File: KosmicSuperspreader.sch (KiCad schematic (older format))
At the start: 22 parts

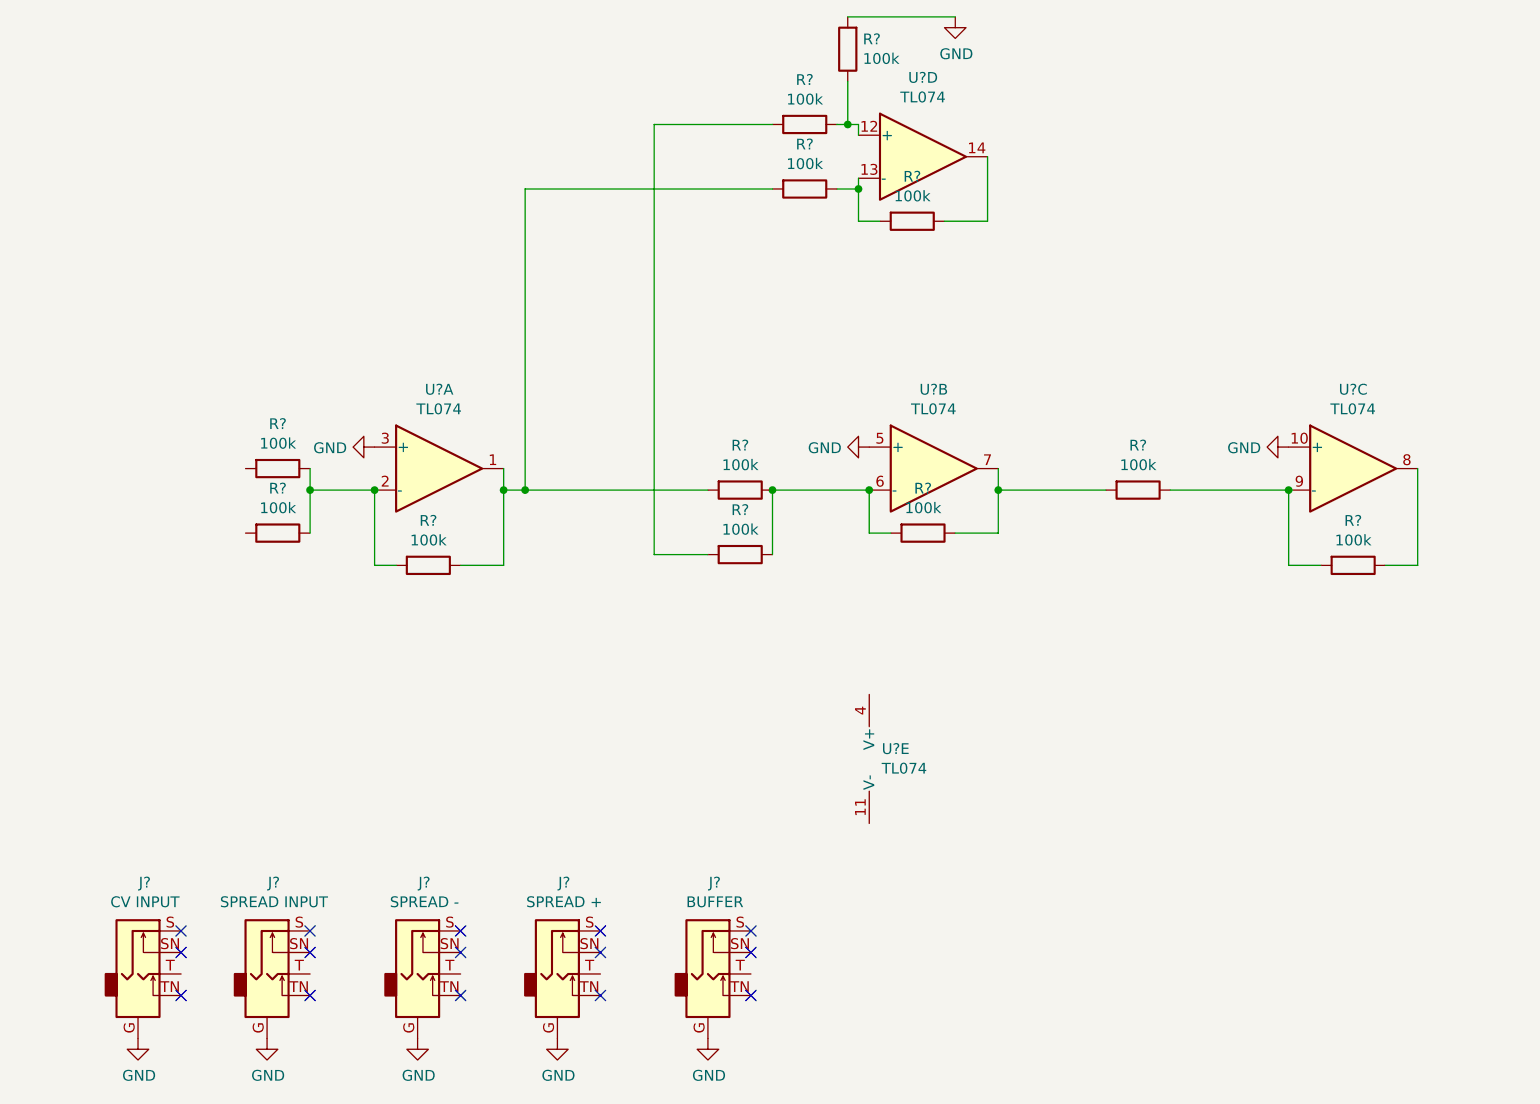
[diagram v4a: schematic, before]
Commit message: Pots and labels
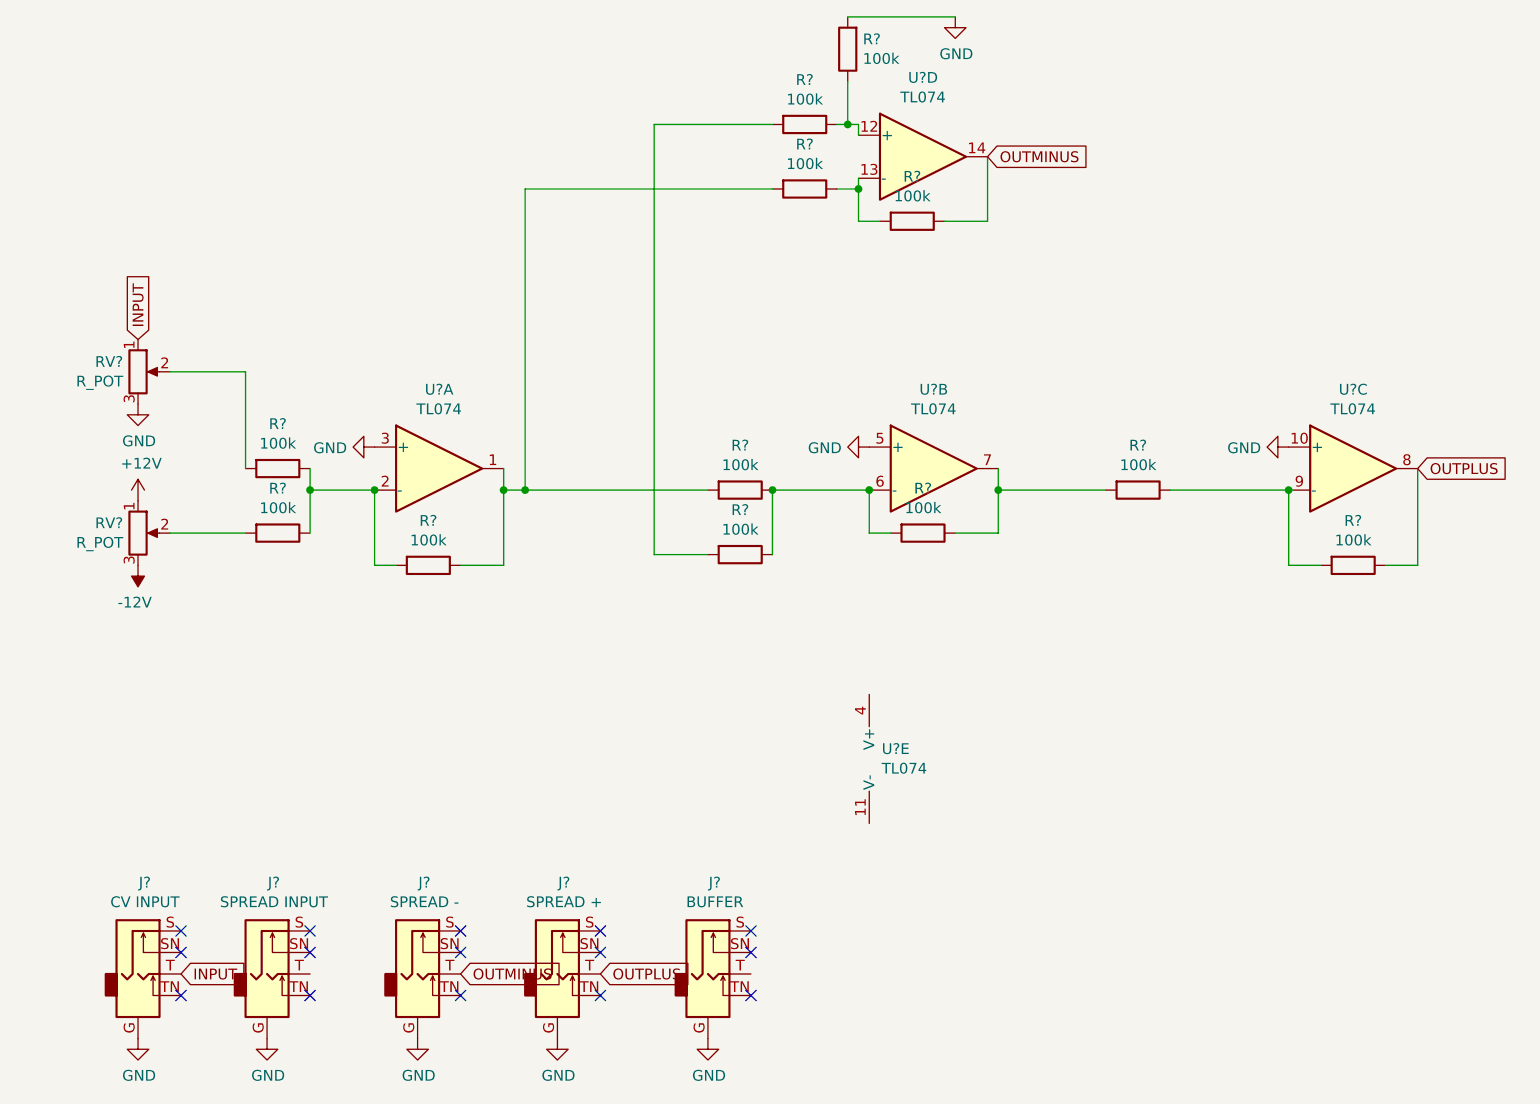
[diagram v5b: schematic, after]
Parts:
- added RV? (x2): R_POT, symbol Device:R_POT
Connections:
- net GND: now also RV?.3
- net OUTPLUS: now reaches R?.1, U?.8
- net OUTPLUS: now also J?.T
- net OUTMINUS: now reaches R?.1, U?.14
- net OUTMINUS: now also J?.T
- net at R?.2: now also RV?.2 (x2)
- net INPUT: now reaches J?.T
- net INPUT: now also RV?.1
- new net +12V: RV?.1
- new net -12V: RV?.3
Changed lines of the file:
@@
 	1    0    0    -1
 $EndComp
+$Comp
+L Device:R_POT RV?
+U 1 1 60B37DC5
+P 1600 4300
+F 0 "RV?" H 1531 4346 50  0000 R CNN
+F 1 "R_POT" H 1531 4255 50  0000 R CNN
+F 2 "" H 1600 4300 50  0001 C CNN
+F 3 "~" H 1600 4300 50  0001 C CNN
+	1    1600 4300
+	1    0    0    -1
+$EndComp
+Text GLabel 7550 4000 2    50   Input ~ 0
+OUTPLUS
+Text GLabel 3750 6350 2    50   Input ~ 0
+OUTPLUS
+Text GLabel 5550 2550 2    50   Input ~ 0
+OUTMINUS
+Text GLabel 3100 6350 2    50   Input ~ 0
+OUTMINUS
+$Comp
+L power:-12V #PWR?
+U 1 1 60B39192
+P 1600 4450
+F 0 "#PWR?" H 1600 4550 50  0001 C CNN
+F 1 "-12V" H 1615 4623 50  0000 C CNN
+F 2 "" H 1600 4450 50  0001 C CNN
+F 3 "" H 1600 4450 50  0001 C CNN
+	1    1600 4450
+	-1   0    0    1
+$EndComp
+$Comp
+L power:+12V #PWR?
+U 1 1 60B39B80
+P 1600 4150
+F 0 "#PWR?" H 1600 4000 50  0001 C CNN
+F 1 "+12V" H 1615 4323 50  0000 C CNN
+F 2 "" H 1600 4150 50  0001 C CNN
+F 3 "" H 1600 4150 50  0001 C CNN
+	1    1600 4150
+	1    0    0    -1
+$EndComp
+Wire Wire Line
+	2100 4300 1750 4300
+$Comp
+L Device:R_POT RV?
+U 1 1 60B3AD55
+P 1600 3550
+F 0 "RV?" H 1531 3596 50  0000 R CNN
+F 1 "R_POT" H 1531 3505 50  0000 R CNN
+F 2 "" H 1600 3550 50  0001 C CNN
+F 3 "~" H 1600 3550 50  0001 C CNN
+	1    1600 3550
+	1    0    0    -1
+$EndComp
+$Comp
+L power:GND #PWR?
+U 1 1 60B3B35D
+P 1600 3700
+F 0 "#PWR?" H 1600 3450 50  0001 C CNN
+F 1 "GND" H 1605 3527 50  0000 C CNN
+F 2 "" H 1600 3700 50  0001 C CNN
+F 3 "" H 1600 3700 50  0001 C CNN
+	1    1600 3700
+	1    0    0    -1
+$EndComp
+Text GLabel 1600 3400 1    50   Input ~ 0
+INPUT
+Text GLabel 1800 6350 2    50   Input ~ 0
+INPUT
+Wire Wire Line
+	1750 3550 2100 3550
+Wire Wire Line
+	2100 3550 2100 4000
 $EndSCHEMATC

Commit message: Change jacks, fix labels
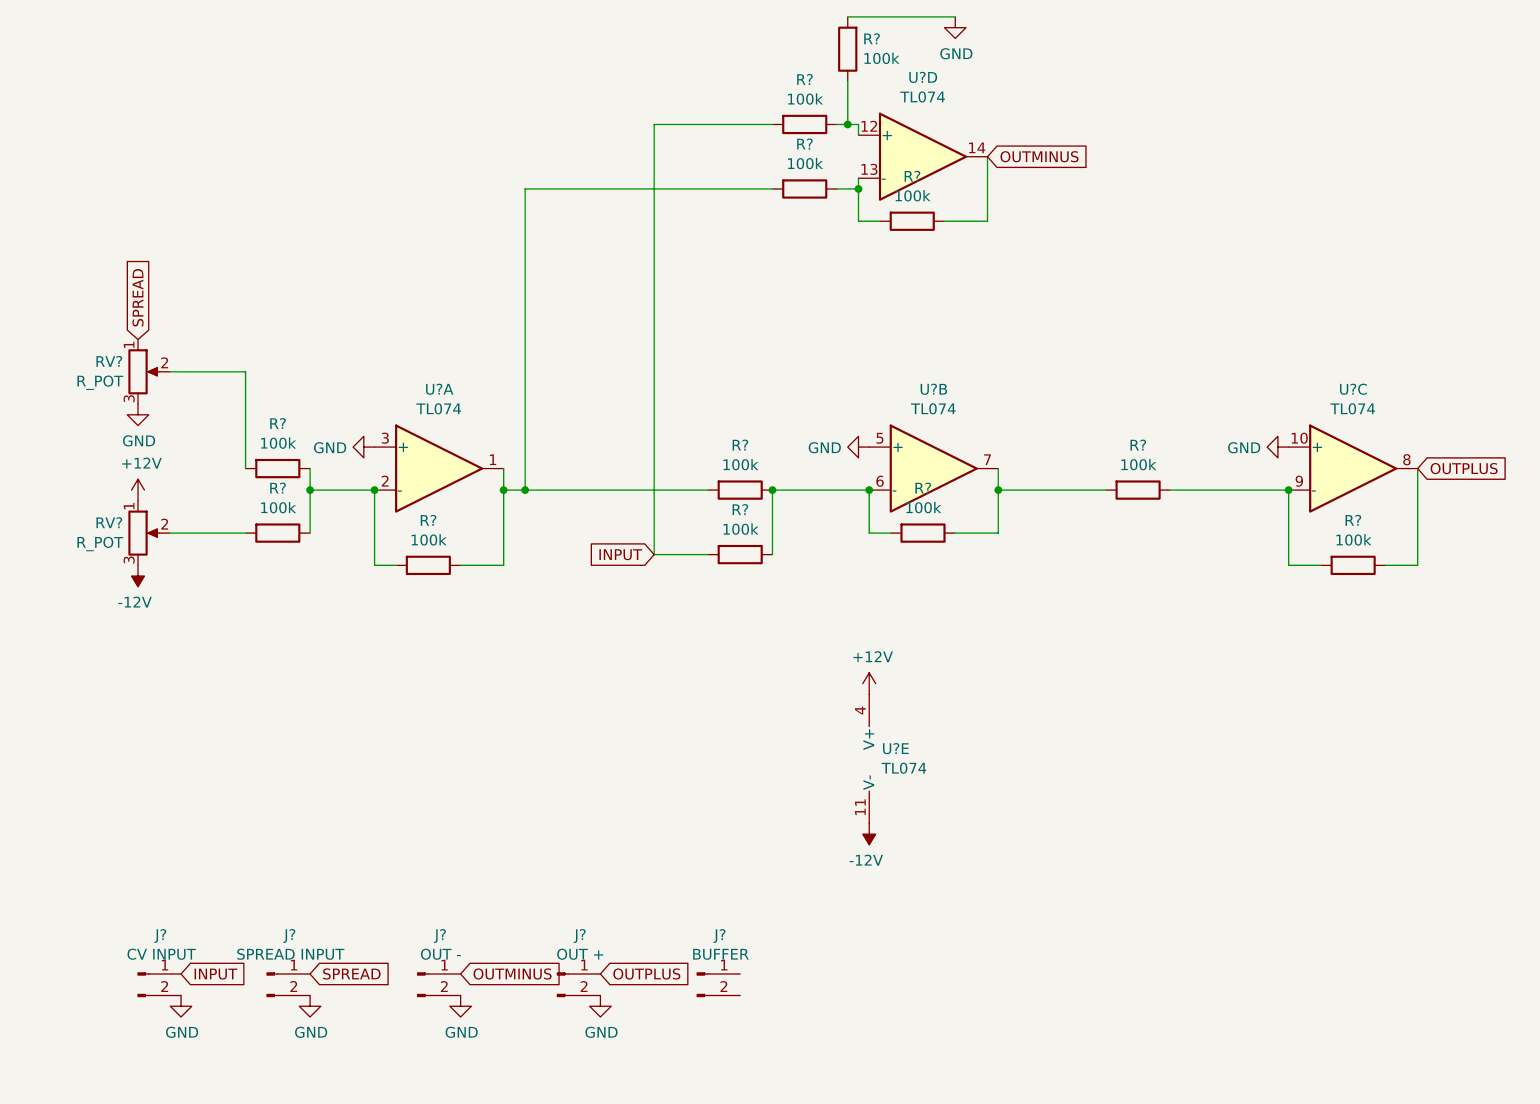
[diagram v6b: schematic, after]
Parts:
- removed J?: SPREAD INPUT, symbol Connector:AudioJack2_Ground_Switch
- removed J?: SPREAD -, symbol Connector:AudioJack2_Ground_Switch
- removed J?: SPREAD +, symbol Connector:AudioJack2_Ground_Switch
- removed J?: BUFFER, symbol Connector:AudioJack2_Ground_Switch
- removed J?: CV INPUT, symbol Connector:AudioJack2_Ground_Switch
- added J?: CV INPUT, symbol Connector:Conn_01x02_Male
- added J?: SPREAD INPUT, symbol Connector:Conn_01x02_Male
- added J?: OUT -, symbol Connector:Conn_01x02_Male
- added J?: OUT +, symbol Connector:Conn_01x02_Male
- added J?: BUFFER, symbol Connector:Conn_01x02_Male
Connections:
- net +12V: now also U?.4 (V+)
- net -12V: now also U?.11 (V-)
- net GND: now also J?.2 (Pin_2), J?.2 (Pin_2), J?.2 (Pin_2), J?.2 (Pin_2)
- net INPUT: now also R?.2, R?.2, J?.1 (Pin_1); no longer RV?.1
- net OUTMINUS: now also J?.1 (Pin_1)
- net OUTPLUS: now also J?.1 (Pin_1)
- new net SPREAD: J?.1 (Pin_1), RV?.1
- no-connect marks 15 -> 0
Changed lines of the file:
@@
 	4000 2400 4550 2400
 $Comp
-L Connector:AudioJack2_Ground_Switch J?
-U 1 1 60B2E747
-P 2200 6350
-F 0 "J?" H 2232 6775 50  0000 C CNN
-F 1 "SPREAD INPUT" H 2232 6684 50  0000 C CNN
-F 2 "" H 2200 6550 50  0001 C CNN
-F 3 "~" H 2200 6550 50  0001 C CNN
-F 4 "A-1121" H 2200 6350 50  0001 C CNN "Part"
-	1    2200 6350
-	1    0    0    -1
-$EndComp
-NoConn ~ 2400 6450
-NoConn ~ 2400 6250
-NoConn ~ 2400 6150
-$Comp
-L power:GND #PWR?
-U 1 1 60B30BB2
-P 2200 6650
-F 0 "#PWR?" H 2200 6400 50  0001 C CNN
-F 1 "GND" H 2205 6477 50  0000 C CNN
-F 2 "" H 2200 6650 50  0001 C CNN
-F 3 "" H 2200 6650 50  0001 C CNN
-	1    2200 6650
-	1    0    0    -1
-$EndComp
-$Comp
-L Connector:AudioJack2_Ground_Switch J?
-U 1 1 60B31450
-P 2900 6350
-F 0 "J?" H 2932 6775 50  0000 C CNN
-F 1 "SPREAD -" H 2932 6684 50  0000 C CNN
-F 2 "" H 2900 6550 50  0001 C CNN
-F 3 "~" H 2900 6550 50  0001 C CNN
-F 4 "A-1121" H 2900 6350 50  0001 C CNN "Part"
-	1    2900 6350
-	1    0    0    -1
-$EndComp
-NoConn ~ 3100 6450
-NoConn ~ 3100 6250
-NoConn ~ 3100 6150
-$Comp
-L power:GND #PWR?
-U 1 1 60B31769
-P 2900 6650
-F 0 "#PWR?" H 2900 6400 50  0001 C CNN
-F 1 "GND" H 2905 6477 50  0000 C CNN
-F 2 "" H 2900 6650 50  0001 C CNN
-F 3 "" H 2900 6650 50  0001 C CNN
-	1    2900 6650
-	1    0    0    -1
-$EndComp
-$Comp
-L Connector:AudioJack2_Ground_Switch J?
-U 1 1 60B33779
-P 3550 6350
-F 0 "J?" H 3582 6775 50  0000 C CNN
-F 1 "SPREAD +" H 3582 6684 50  0000 C CNN
-F 2 "" H 3550 6550 50  0001 C CNN
-F 3 "~" H 3550 6550 50  0001 C CNN
-F 4 "A-1121" H 3550 6350 50  0001 C CNN "Part"
-	1    3550 6350
-	1    0    0    -1
-$EndComp
-NoConn ~ 3750 6450
-NoConn ~ 3750 6250
-NoConn ~ 3750 6150
-$Comp
-L power:GND #PWR?
-U 1 1 60B33AC2
-P 3550 6650
-F 0 "#PWR?" H 3550 6400 50  0001 C CNN
-F 1 "GND" H 3555 6477 50  0000 C CNN
-F 2 "" H 3550 6650 50  0001 C CNN
-F 3 "" H 3550 6650 50  0001 C CNN
-	1    3550 6650
-	1    0    0    -1
-$EndComp
-$Comp
-L Connector:AudioJack2_Ground_Switch J?
-U 1 1 60B33ACD
-P 4250 6350
-F 0 "J?" H 4282 6775 50  0000 C CNN
-F 1 "BUFFER" H 4282 6684 50  0000 C CNN
-F 2 "" H 4250 6550 50  0001 C CNN
-F 3 "~" H 4250 6550 50  0001 C CNN
-F 4 "A-1121" H 4250 6350 50  0001 C CNN "Part"
-	1    4250 6350
-	1    0    0    -1
-$EndComp
-NoConn ~ 4450 6450
-NoConn ~ 4450 6250
-NoConn ~ 4450 6150
-$Comp
-L power:GND #PWR?
-U 1 1 60B33ADA
-P 4250 6650
-F 0 "#PWR?" H 4250 6400 50  0001 C CNN
-F 1 "GND" H 4255 6477 50  0000 C CNN
-F 2 "" H 4250 6650 50  0001 C CNN
-F 3 "" H 4250 6650 50  0001 C CNN
-	1    4250 6650
-	1    0    0    -1
-$EndComp
-$Comp
-L Connector:AudioJack2_Ground_Switch J?
-U 1 1 60B3629C
-P 1600 6350
-F 0 "J?" H 1632 6775 50  0000 C CNN
-F 1 "CV INPUT" H 1632 6684 50  0000 C CNN
-F 2 "" H 1600 6550 50  0001 C CNN
-F 3 "~" H 1600 6550 50  0001 C CNN
-F 4 "A-1121" H 1600 6350 50  0001 C CNN "Part"
-	1    1600 6350
-	1    0    0    -1
-$EndComp
-NoConn ~ 1800 6450
-NoConn ~ 1800 6250
-NoConn ~ 1800 6150
-$Comp
 L power:GND #PWR?
 U 1 1 60B36645
-P 1600 6650
-F 0 "#PWR?" H 1600 6400 50  0001 C CNN
-F 1 "GND" H 1605 6477 50  0000 C CNN
-F 2 "" H 1600 6650 50  0001 C CNN
-F 3 "" H 1600 6650 50  0001 C CNN
-	1    1600 6650
+P 1800 6450
+F 0 "#PWR?" H 1800 6200 50  0001 C CNN
+F 1 "GND" H 1805 6277 50  0000 C CNN
+F 2 "" H 1800 6450 50  0001 C CNN
+F 3 "" H 1800 6450 50  0001 C CNN
+	1    1800 6450
 	1    0    0    -1
 $EndComp
@@
 Text GLabel 7550 4000 2    50   Input ~ 0
 OUTPLUS
-Text GLabel 3750 6350 2    50   Input ~ 0
-OUTPLUS
 Text GLabel 5550 2550 2    50   Input ~ 0
-OUTMINUS
-Text GLabel 3100 6350 2    50   Input ~ 0
 OUTMINUS
 $Comp
@@
 	1    0    0    -1
 $EndComp
-Text GLabel 1600 3400 1    50   Input ~ 0
-INPUT
-Text GLabel 1800 6350 2    50   Input ~ 0
-INPUT
 Wire Wire Line
 	1750 3550 2100 3550
 Wire Wire Line
 	2100 3550 2100 4000
+Text GLabel 1800 6350 2    50   Input ~ 0
+INPUT
+Text GLabel 3100 6350 2    50   Input ~ 0
+OUTMINUS
+Text GLabel 3750 6350 2    50   Input ~ 0
+OUTPLUS
+$Comp
+L Connector:Conn_01x02_Male J?
+U 1 1 60B41A70
+P 1600 6350
+F 0 "J?" H 1708 6531 50  0000 C CNN
+F 1 "CV INPUT" H 1708 6440 50  0000 C CNN
+F 2 "" H 1600 6350 50  0001 C CNN
+F 3 "~" H 1600 6350 50  0001 C CNN
+	1    1600 6350
+	1    0    0    -1
+$EndComp
+$Comp
+L Connector:Conn_01x02_Male J?
+U 1 1 60B4215E
+P 2200 6350
+F 0 "J?" H 2308 6531 50  0000 C CNN
+F 1 "SPREAD INPUT" H 2308 6440 50  0000 C CNN
+F 2 "" H 2200 6350 50  0001 C CNN
+F 3 "~" H 2200 6350 50  0001 C CNN
+	1    2200 6350
+	1    0    0    -1
+$EndComp
+$Comp
+L Connector:Conn_01x02_Male J?
+U 1 1 60B425A1
+P 2900 6350
+F 0 "J?" H 3008 6531 50  0000 C CNN
+F 1 "OUT -" H 3008 6440 50  0000 C CNN
+F 2 "" H 2900 6350 50  0001 C CNN
+F 3 "~" H 2900 6350 50  0001 C CNN
+	1    2900 6350
+	1    0    0    -1
+$EndComp
+$Comp
+L Connector:Conn_01x02_Male J?
+U 1 1 60B42AEE
+P 3550 6350
+F 0 "J?" H 3658 6531 50  0000 C CNN
+F 1 "OUT +" H 3658 6440 50  0000 C CNN
+F 2 "" H 3550 6350 50  0001 C CNN
+F 3 "~" H 3550 6350 50  0001 C CNN
+	1    3550 6350
+	1    0    0    -1
+$EndComp
+$Comp
+L Connector:Conn_01x02_Male J?
+U 1 1 60B42F56
+P 4200 6350
+F 0 "J?" H 4308 6531 50  0000 C CNN
+F 1 "BUFFER" H 4308 6440 50  0000 C CNN
+F 2 "" H 4200 6350 50  0001 C CNN
+F 3 "~" H 4200 6350 50  0001 C CNN
+	1    4200 6350
+	1    0    0    -1
+$EndComp
+$Comp
+L power:GND #PWR?
+U 1 1 60B441EE
+P 2400 6450
+F 0 "#PWR?" H 2400 6200 50  0001 C CNN
+F 1 "GND" H 2405 6277 50  0000 C CNN
+F 2 "" H 2400 6450 50  0001 C CNN
+F 3 "" H 2400 6450 50  0001 C CNN
+	1    2400 6450
+	1    0    0    -1
+$EndComp
+$Comp
+L power:GND #PWR?
+U 1 1 60B444E3
+P 3100 6450
+F 0 "#PWR?" H 3100 6200 50  0001 C CNN
+F 1 "GND" H 3105 6277 50  0000 C CNN
+F 2 "" H 3100 6450 50  0001 C CNN
+F 3 "" H 3100 6450 50  0001 C CNN
+	1    3100 6450
+	1    0    0    -1
+$EndComp
+Text GLabel 1600 3400 1    50   Input ~ 0
+SPREAD
+Text GLabel 2400 6350 2    50   Input ~ 0
+SPREAD
+Text GLabel 4000 4400 0    50   Input ~ 0
+INPUT
+$Comp
+L power:GND #PWR?
+U 1 1 60B453F6
+P 3750 6450
+F 0 "#PWR?" H 3750 6200 50  0001 C CNN
+F 1 "GND" H 3755 6277 50  0000 C CNN
+F 2 "" H 3750 6450 50  0001 C CNN
+F 3 "" H 3750 6450 50  0001 C CNN
+	1    3750 6450
+	1    0    0    -1
+$EndComp
+$Comp
+L power:+12V #PWR?
+U 1 1 60B4570D
+P 5000 5050
+F 0 "#PWR?" H 5000 4900 50  0001 C CNN
+F 1 "+12V" H 5015 5223 50  0000 C CNN
+F 2 "" H 5000 5050 50  0001 C CNN
+F 3 "" H 5000 5050 50  0001 C CNN
+	1    5000 5050
+	1    0    0    -1
+$EndComp
+$Comp
+L power:-12V #PWR?
+U 1 1 60B45CE9
+P 5000 5650
+F 0 "#PWR?" H 5000 5750 50  0001 C CNN
+F 1 "-12V" H 5015 5823 50  0000 C CNN
+F 2 "" H 5000 5650 50  0001 C CNN
+F 3 "" H 5000 5650 50  0001 C CNN
+	1    5000 5650
+	-1   0    0    1
+$EndComp
 $EndSCHEMATC

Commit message: Buffer
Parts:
- added U?: TL072, symbol Amplifier_Operational:TL072
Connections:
- net GND: now also J?.2 (Pin_2)
- net INPUT: now also U?.3 (+)
- net OUTPUT: now reaches J?.1 (Pin_1)
- net OUTPUT: now also U?.1, U?.2 (-)
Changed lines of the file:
@@
 	-1   0    0    1
 $EndComp
+$Comp
+L Amplifier_Operational:TL072 U?
+U 1 1 60B46627
+P 6800 5400
+F 0 "U?" H 6800 5767 50  0000 C CNN
+F 1 "TL072" H 6800 5676 50  0000 C CNN
+F 2 "" H 6800 5400 50  0001 C CNN
+F 3 "http://www.ti.com/lit/ds/symlink/tl071.pdf" H 6800 5400 50  0001 C CNN
+	1    6800 5400
+	1    0    0    -1
+$EndComp
+Wire Wire Line
+	6500 5500 6500 5650
+Wire Wire Line
+	6500 5650 7100 5650
+Wire Wire Line
+	7100 5650 7100 5400
+Text GLabel 6500 5300 0    50   Input ~ 0
+INPUT
+Text GLabel 7100 5400 2    50   Input ~ 0
+OUTPUT
+Text GLabel 4400 6350 2    50   Input ~ 0
+OUTPUT
+$Comp
+L power:GND #PWR?
+U 1 1 60B4B8F2
+P 4400 6450
+F 0 "#PWR?" H 4400 6200 50  0001 C CNN
+F 1 "GND" H 4405 6277 50  0000 C CNN
+F 2 "" H 4400 6450 50  0001 C CNN
+F 3 "" H 4400 6450 50  0001 C CNN
+	1    4400 6450
+	1    0    0    -1
+$EndComp
 $EndSCHEMATC

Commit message: Decoupling
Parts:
- added C? (x2): C_Small, symbol Device:C_Small
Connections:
- net +12V: now also C?.1
- net -12V: now also C?.1
- net GND: now also C?.2, C?.2
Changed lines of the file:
@@
 	1    0    0    -1
 $EndComp
+$Comp
+L Device:C_Small C?
+U 1 1 60B4C0F4
+P 5100 5050
+F 0 "C?" V 5329 5050 50  0000 C CNN
+F 1 "C_Small" V 5238 5050 50  0000 C CNN
+F 2 "" H 5100 5050 50  0001 C CNN
+F 3 "~" H 5100 5050 50  0001 C CNN
+	1    5100 5050
+	0    -1   -1   0
+$EndComp
+Connection ~ 5000 5050
+$Comp
+L Device:C_Small C?
+U 1 1 60B4CBBF
+P 5100 5650
+F 0 "C?" V 5329 5650 50  0000 C CNN
+F 1 "C_Small" V 5238 5650 50  0000 C CNN
+F 2 "" H 5100 5650 50  0001 C CNN
+F 3 "~" H 5100 5650 50  0001 C CNN
+	1    5100 5650
+	0    -1   -1   0
+$EndComp
+Connection ~ 5000 5650
+$Comp
+L power:GND #PWR?
+U 1 1 60B4D06F
+P 5450 5300
+F 0 "#PWR?" H 5450 5050 50  0001 C CNN
+F 1 "GND" H 5455 5127 50  0000 C CNN
+F 2 "" H 5450 5300 50  0001 C CNN
+F 3 "" H 5450 5300 50  0001 C CNN
+	1    5450 5300
+	1    0    0    -1
+$EndComp
+Wire Wire Line
+	5200 5050 5450 5050
+Wire Wire Line
+	5450 5050 5450 5300
+Wire Wire Line
+	5200 5650 5300 5650
+Wire Wire Line
+	5300 5650 5300 5300
+Wire Wire Line
+	5300 5300 5450 5300
+Connection ~ 5450 5300
 $EndSCHEMATC
